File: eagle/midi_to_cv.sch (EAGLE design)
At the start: 67 parts, among them IC1 TL082P, IC2 TL084P, IC4 TL082P, IC6 TL082P, IC7 TL082P, U1 ATMEGA328P_PDIP, U2 MCP4822-E/P, U3 MCP4822-E/P, U4 MCP4822-E/P, U5 MCP4822-E/P

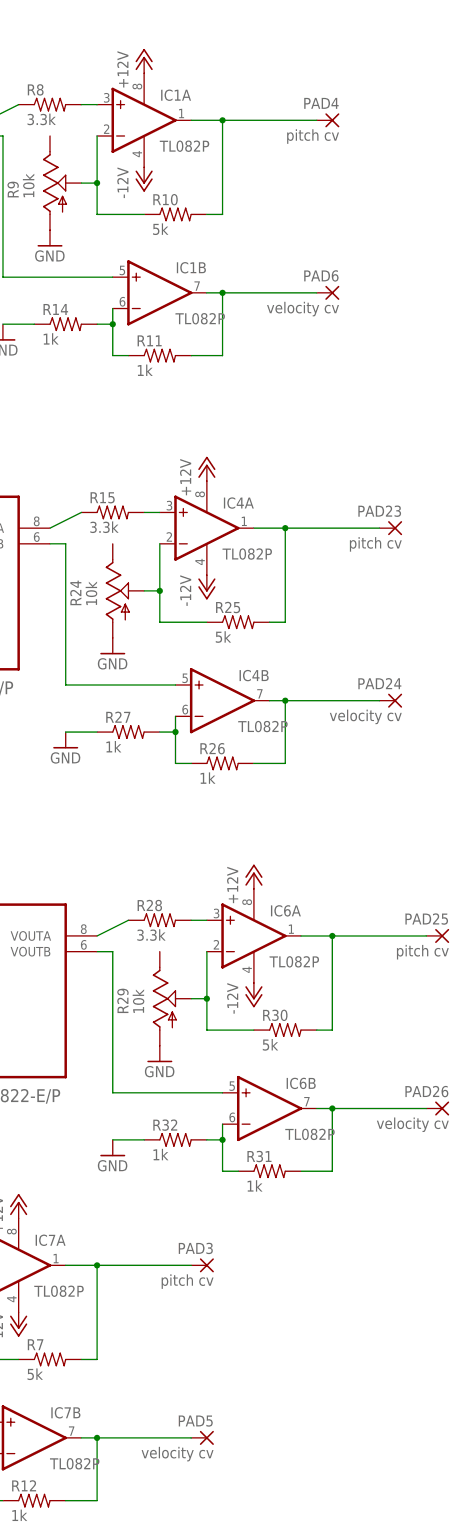
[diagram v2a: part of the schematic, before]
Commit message: updated arduino code
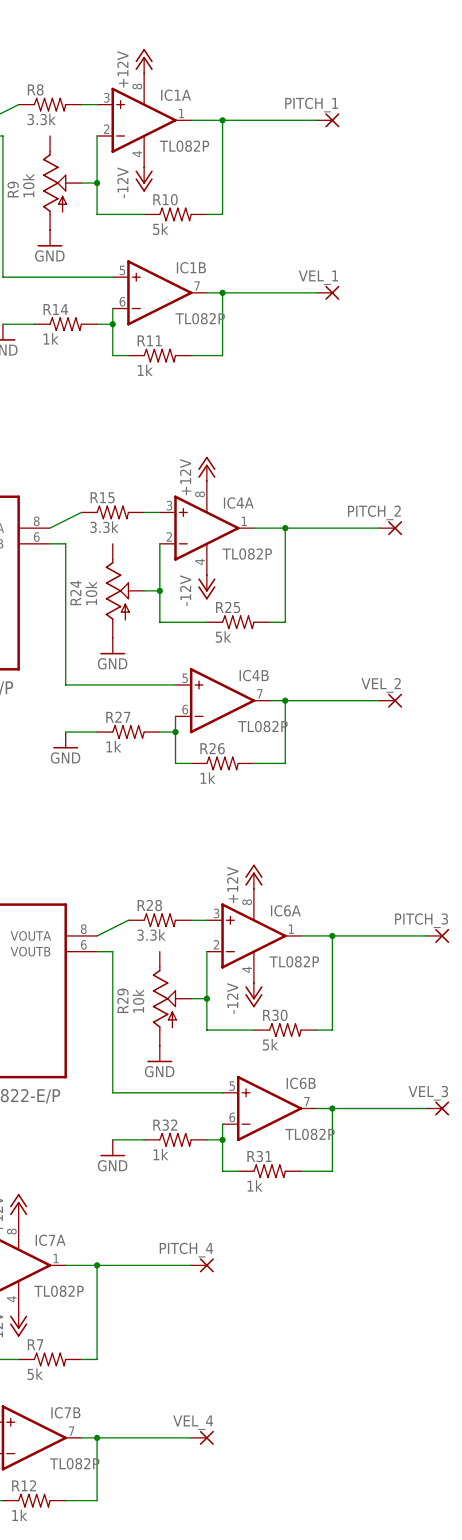
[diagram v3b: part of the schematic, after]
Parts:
- PITCH_1, PITCH_2, PITCH_3, PITCH_4: value pitch cv -> (none)
- VEL_1, VEL_2, VEL_3, VEL_4: value velocity cv -> (none)
- renumbered PAD23 to PITCH_2, PAD24 to VEL_2, PAD25 to PITCH_3, PAD26 to VEL_3, PAD3 to PITCH_4, PAD4 to PITCH_1, PAD5 to VEL_4, PAD6 to VEL_1
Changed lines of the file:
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@@
 <part name="R6" library="pot" deviceset="TRIM_US-" device="B64W" value="10k"/>
 <part name="GND4" library="supply1" deviceset="GND" device=""/>
-<part name="PAD3" library="wirepad" deviceset="2,54/0,9" device="" value="pitch cv"/>
+<part name="PITCH_4" library="wirepad" deviceset="2,54/0,9" device=""/>
 <part name="R7" library="rcl" deviceset="R-US_" device="0207/10" value="5k"/>
 <part name="R12" library="rcl" deviceset="R-US_" device="0207/10" value="1k"/>
 <part name="R13" library="rcl" deviceset="R-US_" device="0207/10" value="1k"/>
 <part name="GND6" library="supply1" deviceset="GND" device=""/>
-<part name="PAD5" library="wirepad" deviceset="2,54/0,9" device="" value="velocity cv"/>
+<part name="VEL_4" library="wirepad" deviceset="2,54/0,9" device=""/>
 <part name="P+6" library="supply1" deviceset="+5V" device=""/>
 <part name="U4" library="MCP4822" deviceset="MCP4822-E/P" device=""/>
@@
 <part name="R9" library="pot" deviceset="TRIM_US-" device="B64W" value="10k"/>
 <part name="GND7" library="supply1" deviceset="GND" device=""/>
-<part name="PAD4" library="wirepad" deviceset="2,54/0,9" device="" value="pitch cv"/>
+<part name="PITCH_1" library="wirepad" deviceset="2,54/0,9" device=""/>
 <part name="R10" library="rcl" deviceset="R-US_" device="0207/10" value="5k"/>
 <part name="R11" library="rcl" deviceset="R-US_" device="0207/10" value="1k"/>
 <part name="R14" library="rcl" deviceset="R-US_" device="0207/10" value="1k"/>
 <part name="GND10" library="supply1" deviceset="GND" device=""/>
-<part name="PAD6" library="wirepad" deviceset="2,54/0,9" device="" value="velocity cv"/>
+<part name="VEL_1" library="wirepad" deviceset="2,54/0,9" device=""/>
 <part name="P+5" library="supply1" deviceset="+5V" device=""/>
 <part name="U2" library="MCP4822" deviceset="MCP4822-E/P" device=""/>
@@
 <part name="R24" library="pot" deviceset="TRIM_US-" device="B64W" value="10k"/>
 <part name="GND13" library="supply1" deviceset="GND" device=""/>
-<part name="PAD23" library="wirepad" deviceset="2,54/0,9" device="" value="pitch cv"/>
+<part name="PITCH_2" library="wirepad" deviceset="2,54/0,9" device=""/>
 <part name="R25" library="rcl" deviceset="R-US_" device="0207/10" value="5k"/>
 <part name="R26" library="rcl" deviceset="R-US_" device="0207/10" value="1k"/>
 <part name="R27" library="rcl" deviceset="R-US_" device="0207/10" value="1k"/>
 <part name="GND14" library="supply1" deviceset="GND" device=""/>
-<part name="PAD24" library="wirepad" deviceset="2,54/0,9" device="" value="velocity cv"/>
+<part name="VEL_2" library="wirepad" deviceset="2,54/0,9" device=""/>
 <part name="P+10" library="supply1" deviceset="+5V" device=""/>
 <part name="U3" library="MCP4822" deviceset="MCP4822-E/P" device=""/>
@@
 <part name="R29" library="pot" deviceset="TRIM_US-" device="B64W" value="10k"/>
 <part name="GND16" library="supply1" deviceset="GND" device=""/>
-<part name="PAD25" library="wirepad" deviceset="2,54/0,9" device="" value="pitch cv"/>
+<part name="PITCH_3" library="wirepad" deviceset="2,54/0,9" device=""/>
 <part name="R30" library="rcl" deviceset="R-US_" device="0207/10" value="5k"/>
 <part name="R31" library="rcl" deviceset="R-US_" device="0207/10" value="1k"/>
 <part name="R32" library="rcl" deviceset="R-US_" device="0207/10" value="1k"/>
 <part name="GND17" library="supply1" deviceset="GND" device=""/>
-<part name="PAD26" library="wirepad" deviceset="2,54/0,9" device="" value="velocity cv"/>
+<part name="VEL_3" library="wirepad" deviceset="2,54/0,9" device=""/>
 <part name="P+12" library="supply1" deviceset="+5V" device=""/>
 <part name="U5" library="MCP4822" deviceset="MCP4822-E/P" device=""/>
@@
 <instance part="R6" gate="G$1" x="157.48" y="-73.66"/>
 <instance part="GND4" gate="1" x="157.48" y="-83.82"/>
-<instance part="PAD3" gate="1" x="203.2" y="-63.5" rot="MR0"/>
+<instance part="PITCH_4" gate="1" x="203.2" y="-63.5" rot="MR0"/>
 <instance part="R7" gate="G$1" x="177.8" y="-78.74"/>
 <instance part="R12" gate="G$1" x="175.26" y="-101.6"/>
 <instance part="R13" gate="G$1" x="160.02" y="-96.52"/>
 <instance part="GND6" gate="1" x="149.86" y="-99.06"/>
-<instance part="PAD5" gate="1" x="203.2" y="-91.44" rot="MR0"/>
+<instance part="VEL_4" gate="1" x="203.2" y="-91.44" rot="MR0"/>
 <instance part="P+6" gate="1" x="109.22" y="-55.88"/>
 <instance part="U4" gate="A" x="129.54" y="-68.58"/>
@@
 <instance part="R9" gate="G$1" x="177.8" y="111.76"/>
 <instance part="GND7" gate="1" x="177.8" y="101.6"/>
-<instance part="PAD4" gate="1" x="223.52" y="121.92" rot="MR0"/>
+<instance part="PITCH_1" gate="1" x="223.52" y="121.92" rot="MR0"/>
 <instance part="R10" gate="G$1" x="198.12" y="106.68"/>
 <instance part="R11" gate="G$1" x="195.58" y="83.82"/>
 <instance part="R14" gate="G$1" x="180.34" y="88.9"/>
 <instance part="GND10" gate="1" x="170.18" y="86.36"/>
-<instance part="PAD6" gate="1" x="223.52" y="93.98" rot="MR0"/>
+<instance part="VEL_1" gate="1" x="223.52" y="93.98" rot="MR0"/>
 <instance part="P+5" gate="1" x="129.54" y="129.54"/>
 <instance part="U2" gate="A" x="149.86" y="116.84"/>
@@
 <instance part="R24" gate="G$1" x="187.96" y="45.72"/>
 <instance part="GND13" gate="1" x="187.96" y="35.56"/>
-<instance part="PAD23" gate="1" x="233.68" y="55.88" rot="MR0"/>
+<instance part="PITCH_2" gate="1" x="233.68" y="55.88" rot="MR0"/>
 <instance part="R25" gate="G$1" x="208.28" y="40.64"/>
 <instance part="R26" gate="G$1" x="205.74" y="17.78"/>
 <instance part="R27" gate="G$1" x="190.5" y="22.86"/>
 <instance part="GND14" gate="1" x="180.34" y="20.32"/>
-<instance part="PAD24" gate="1" x="233.68" y="27.94" rot="MR0"/>
+<instance part="VEL_2" gate="1" x="233.68" y="27.94" rot="MR0"/>
 <instance part="P+10" gate="1" x="139.7" y="63.5"/>
 <instance part="U3" gate="A" x="160.02" y="50.8"/>
@@
 <instance part="R29" gate="G$1" x="195.58" y="-20.32"/>
 <instance part="GND16" gate="1" x="195.58" y="-30.48"/>
-<instance part="PAD25" gate="1" x="241.3" y="-10.16" rot="MR0"/>
+<instance part="PITCH_3" gate="1" x="241.3" y="-10.16" rot="MR0"/>
 <instance part="R30" gate="G$1" x="215.9" y="-25.4"/>
 <instance part="R31" gate="G$1" x="213.36" y="-48.26"/>
 <instance part="R32" gate="G$1" x="198.12" y="-43.18"/>
 <instance part="GND17" gate="1" x="187.96" y="-45.72"/>
-<instance part="PAD26" gate="1" x="241.3" y="-38.1" rot="MR0"/>
+<instance part="VEL_3" gate="1" x="241.3" y="-38.1" rot="MR0"/>
 <instance part="P+12" gate="1" x="147.32" y="-2.54"/>
 <instance part="U5" gate="A" x="167.64" y="-15.24"/>
@@
 <net name="N$9" class="0">
 <segment>
-<pinref part="PAD3" gate="1" pin="P"/>
+<pinref part="PITCH_4" gate="1" pin="P"/>
 <wire x1="180.34" y1="-63.5" x2="185.42" y2="-63.5" width="0.1524" layer="91"/>
 <pinref part="R7" gate="G$1" pin="2"/>
@@
 <pinref part="R12" gate="G$1" pin="2"/>
 <wire x1="185.42" y1="-101.6" x2="180.34" y2="-101.6" width="0.1524" layer="91"/>
-<pinref part="PAD5" gate="1" pin="P"/>
+<pinref part="VEL_4" gate="1" pin="P"/>
 <wire x1="200.66" y1="-91.44" x2="185.42" y2="-91.44" width="0.1524" layer="91"/>
 <junction x="185.42" y="-91.44"/>
@@
 <net name="N$17" class="0">
 <segment>
-<pinref part="PAD4" gate="1" pin="P"/>
+<pinref part="PITCH_1" gate="1" pin="P"/>
 <wire x1="200.66" y1="121.92" x2="205.74" y2="121.92" width="0.1524" layer="91"/>
 <pinref part="R10" gate="G$1" pin="2"/>
@@
 <pinref part="R11" gate="G$1" pin="2"/>
 <wire x1="205.74" y1="83.82" x2="200.66" y2="83.82" width="0.1524" layer="91"/>
-<pinref part="PAD6" gate="1" pin="P"/>
+<pinref part="VEL_1" gate="1" pin="P"/>
 <wire x1="220.98" y1="93.98" x2="205.74" y2="93.98" width="0.1524" layer="91"/>
 <junction x="205.74" y="93.98"/>
@@
 <net name="N$49" class="0">
 <segment>
-<pinref part="PAD23" gate="1" pin="P"/>
+<pinref part="PITCH_2" gate="1" pin="P"/>
 <wire x1="210.82" y1="55.88" x2="215.9" y2="55.88" width="0.1524" layer="91"/>
 <pinref part="R25" gate="G$1" pin="2"/>
@@
 <pinref part="R26" gate="G$1" pin="2"/>
 <wire x1="215.9" y1="17.78" x2="210.82" y2="17.78" width="0.1524" layer="91"/>
-<pinref part="PAD24" gate="1" pin="P"/>
+<pinref part="VEL_2" gate="1" pin="P"/>
 <wire x1="231.14" y1="27.94" x2="215.9" y2="27.94" width="0.1524" layer="91"/>
 <junction x="215.9" y="27.94"/>
@@
 <net name="N$57" class="0">
 <segment>
-<pinref part="PAD25" gate="1" pin="P"/>
+<pinref part="PITCH_3" gate="1" pin="P"/>
 <wire x1="218.44" y1="-10.16" x2="223.52" y2="-10.16" width="0.1524" layer="91"/>
 <pinref part="R30" gate="G$1" pin="2"/>
@@
 <pinref part="R31" gate="G$1" pin="2"/>
 <wire x1="223.52" y1="-48.26" x2="218.44" y2="-48.26" width="0.1524" layer="91"/>
-<pinref part="PAD26" gate="1" pin="P"/>
+<pinref part="VEL_3" gate="1" pin="P"/>
 <wire x1="238.76" y1="-38.1" x2="223.52" y2="-38.1" width="0.1524" layer="91"/>
 <junction x="223.52" y="-38.1"/>
